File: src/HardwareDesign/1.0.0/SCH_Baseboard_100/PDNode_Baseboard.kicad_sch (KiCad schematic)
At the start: 0 parts

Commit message: Baseboard design start
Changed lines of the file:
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@@
 	(paper "A3")
 	(title_block
-		(date "2025-01-12")
+		(date "2026-02-05")
 		(rev "1.0.0")
 		(company "DvidMakesThings")
@@
 	(polyline
 		(pts
-			(xy 241.3 173.99) (xy 243.84 180.34)
+			(xy 241.4932 175.7723) (xy 244.0332 182.1223)
 		)
 		(stroke
@@
 	(polyline
 		(pts
-			(xy 243.84 173.99) (xy 241.3 180.34)
+			(xy 244.0332 175.7723) (xy 241.4932 182.1223)
 		)
 		(stroke
@@
 		)
 		(instances
-			(project "PDNode-600"
+			(project "PDNode_Baseboard"
 				(path "/f9e05184-c88b-4a88-ae9c-ab2bdb32be7c"
 					(page "6")
@@
 		)
 		(instances
-			(project "PDNode-600"
+			(project "PDNode_Baseboard"
 				(path "/f9e05184-c88b-4a88-ae9c-ab2bdb32be7c"
 					(page "2")

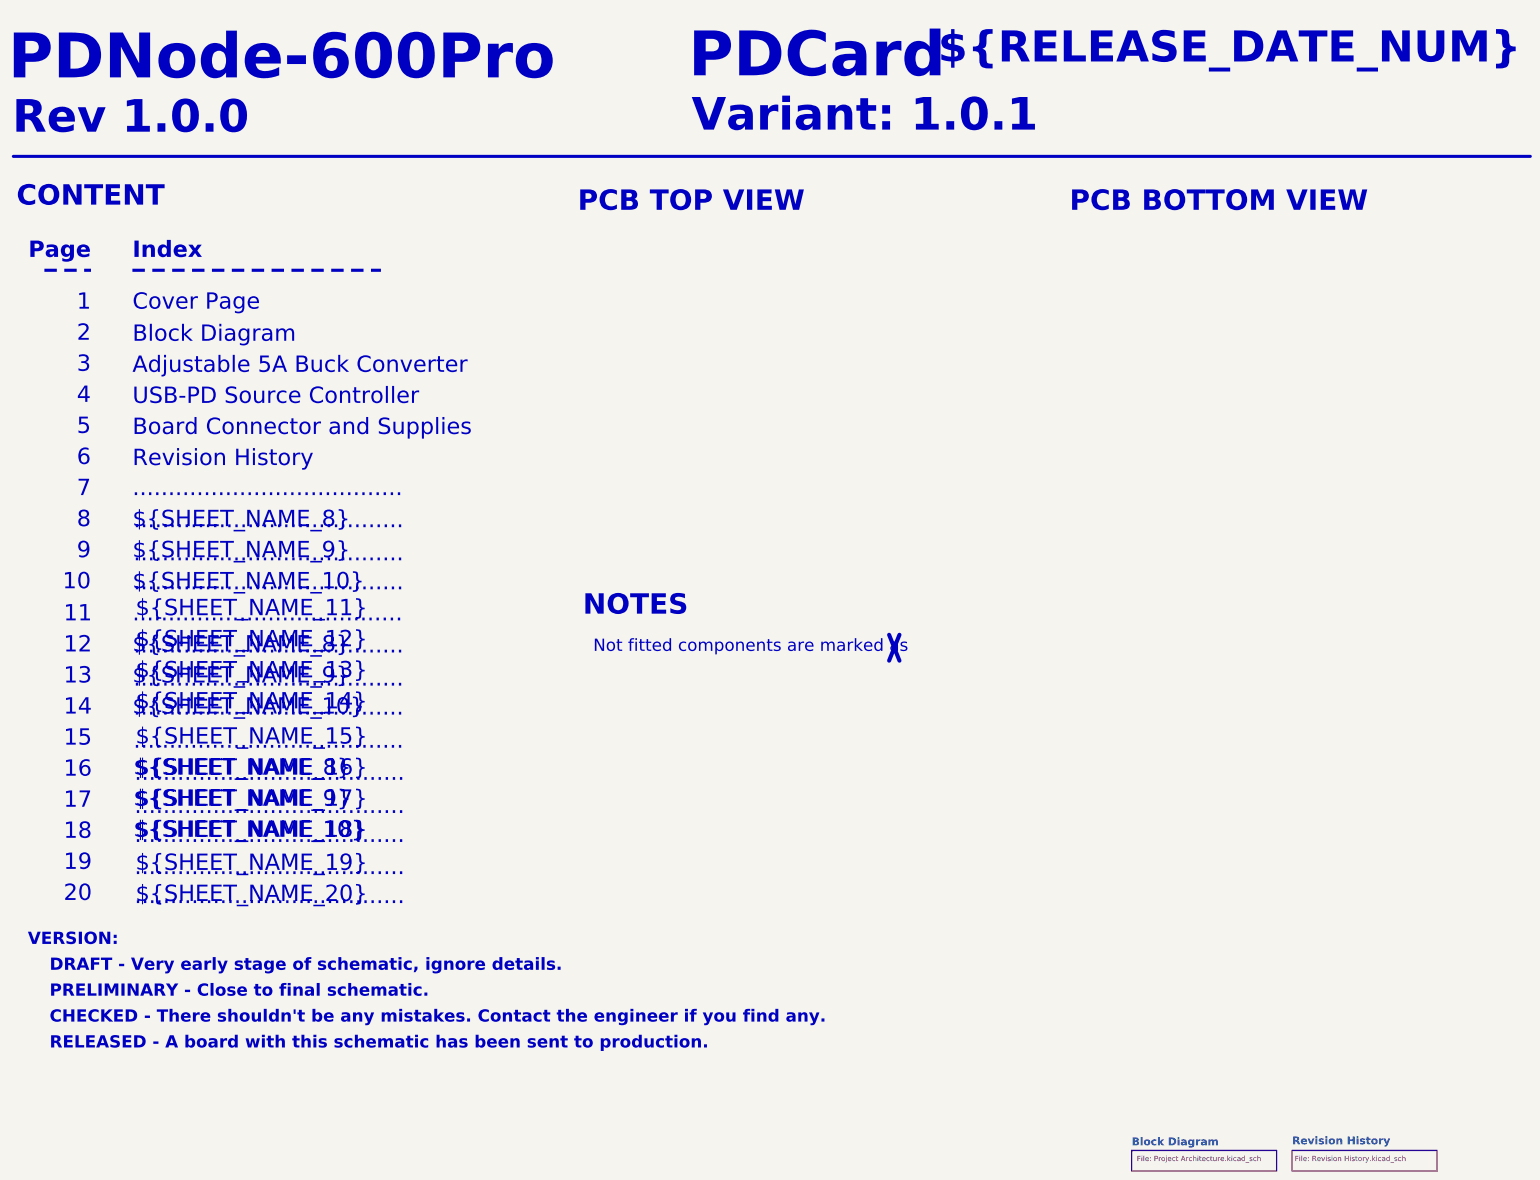
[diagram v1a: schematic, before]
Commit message: Add bladecore to design
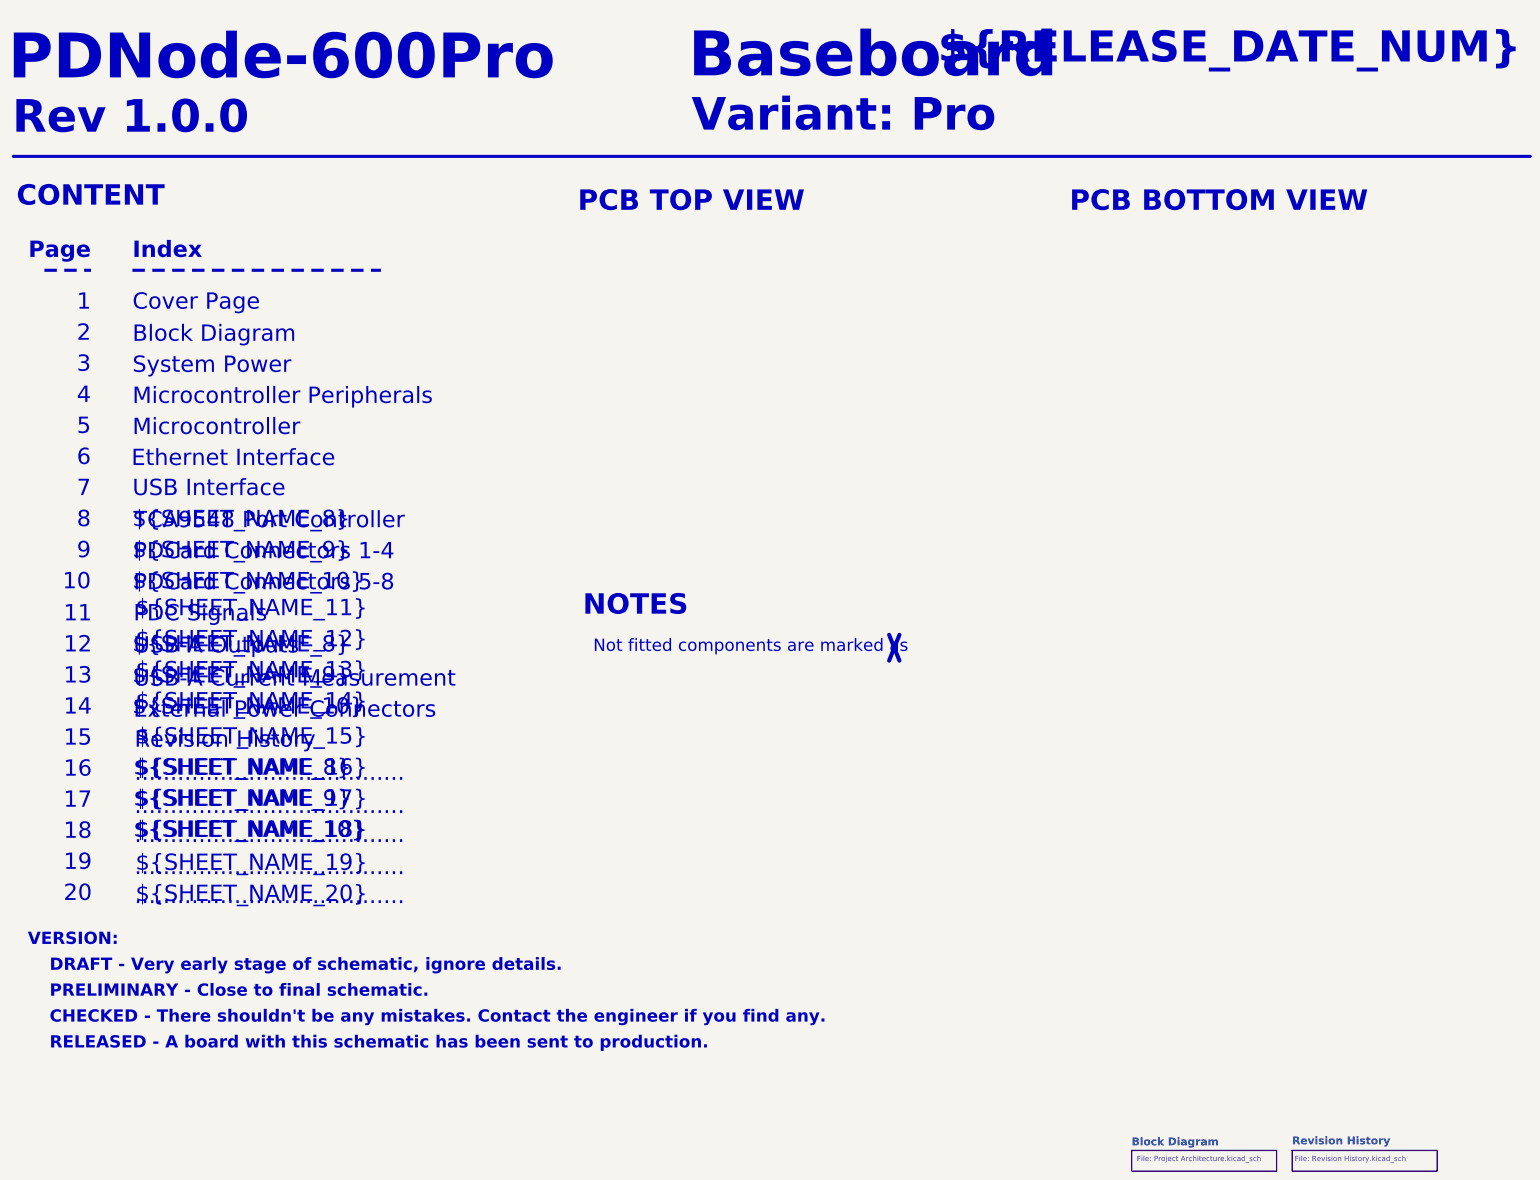
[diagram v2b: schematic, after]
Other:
- note added: "Baseboard"
- note added: "Ethernet Interface"
- note added: "External Power Connectors"
- note added: "Microcontroller"
- note added: "Microcontroller Peripherals"
- note added: "PDC Signals"
- note added: "PDCard Connectors 1-4"
- note added: "PDCard Connectors 5-8"
- note added: "System Power"
- note added: "TCA9548 Port Controller"
- note added: "USB Interface"
- note added: "USB-A Current Measurement"
- note added: "USB-A Outputs"
- note added: "Variant: Pro"
- note removed: "Adjustable 5A Buck Converter"
- note removed: "Board Connector and Supplies"
- note removed: "PDCard"
- note removed: "USB-PD Source Controller"
- note removed: "Variant: 1.0.1"
